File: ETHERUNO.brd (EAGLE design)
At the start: 68.6 x 53.3 mm, 98 parts, among them IC1 MC33269DT-5.0, IC2 APX811-44UG-7, IC3 ATMEGA16U2-MU, IC4 LM358D, IC5 ATMEGA328P TQFP32, IC7 MCP24AA025E48, IC8 W5500, J1 DC_2_1MM, P1 USB-6PSMT, P2 ICSP:MAIN, P3 ICSP:USB, P4 microSD, Q1 FDN340P, Q2 2N7002, Q3 2N7002, U1 HY931147C-RJ45, X1 16MHz, X2 25MHz, X3 16MHz

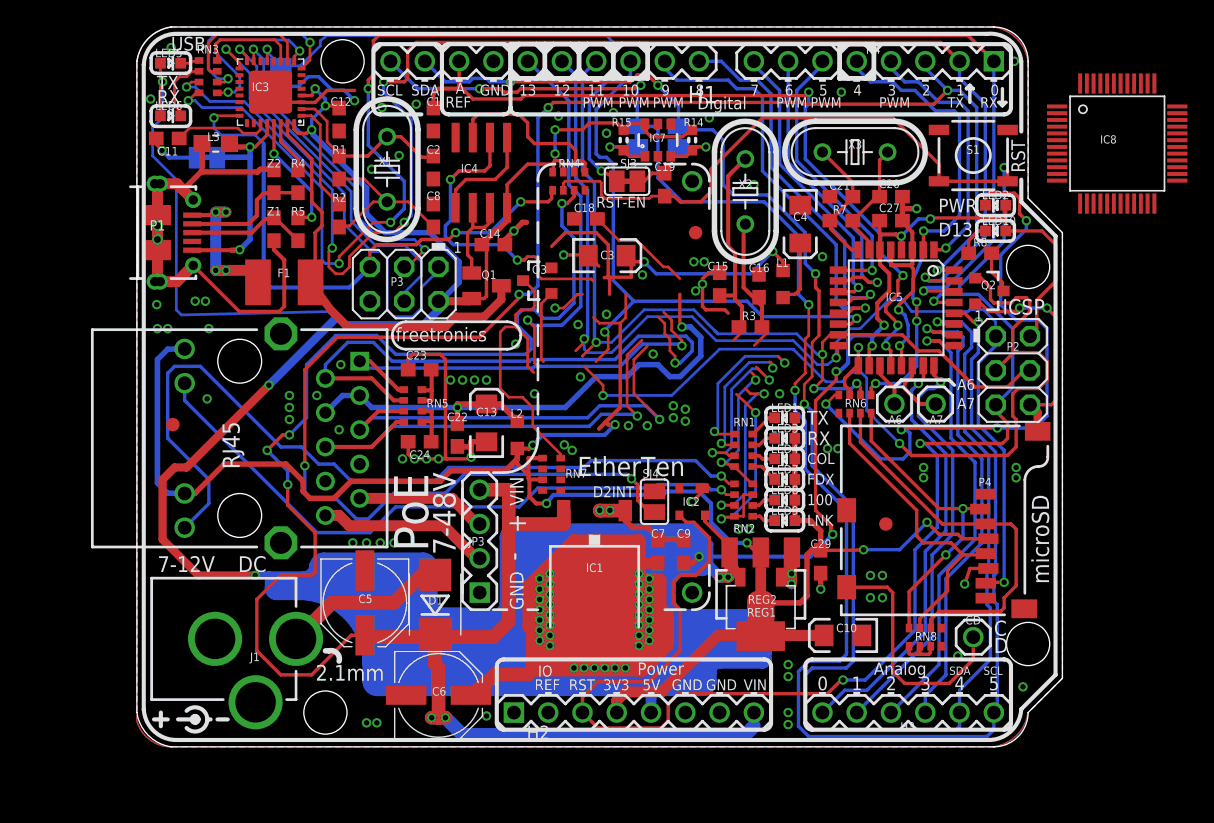
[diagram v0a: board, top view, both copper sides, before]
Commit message: Beginning of conversion to USB-C and W5100S
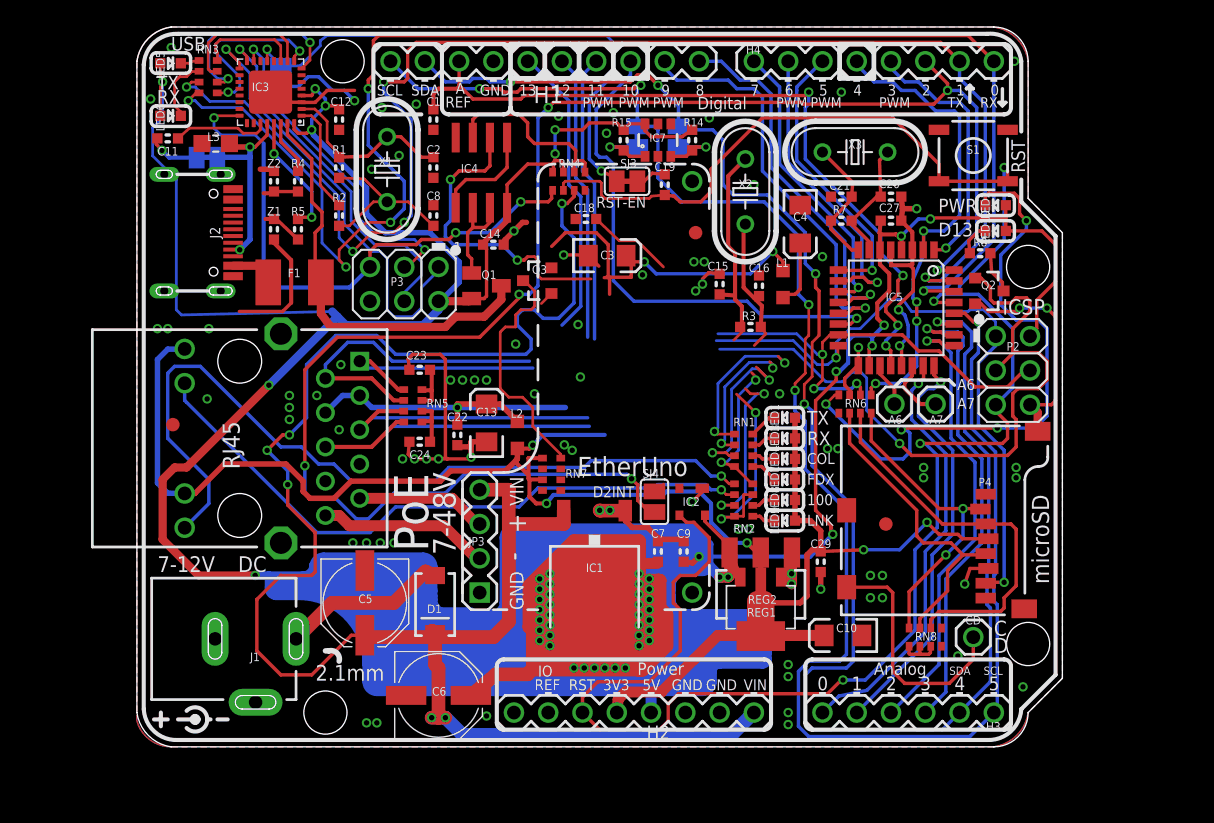
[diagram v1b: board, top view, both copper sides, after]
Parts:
- removed IC8: W5500, W5500:W5500
- removed P1: USB-6PSMT, freetronics-jon:USB-MICROB-MB05PMXX
- added J2: USB-C-16P-16P, SuperHouse-Connectors:USB-C-16P
- C1, C11, C12, C14, C15, C16, C18, C19, C2, C20, C21, C22, C23, C24, C27, C29, C7, C8, C9: device freetronics:0603 -> SuperHouse-DiscreteSemi:C0603
- C10, C13, C3, C4: device freetronics:EIA3216 -> SuperHouse-DiscreteSemi:EIA3216
- C5, C6: device rcl:PANASONIC_D -> SuperHouse-DiscreteSemi:PANASONIC_D
- D1: device freetronics:SMB-DIODE -> SuperHouse-DiscreteSemi:SMA-DIODE
- F1: device rcl:L1812 -> SuperHouse-Fuses:1812
- H1: device freetronics-original:1X10 -> SuperHouse-Connectors:1X10-S
- H2: device freetronics-master-v1:1X08 -> SuperHouse-Connectors:1X08-S
- H3: device freetronics:1X06 -> SuperHouse-Connectors:1X06-S
- H4: device freetronics:1X08 -> SuperHouse-Connectors:1X08-S
- IC5: device freetronics-2:TQFP32-08 -> SuperHouse-MCUs:TQFP32-08
- J1: device freetronics:POWER_JACK_PTH -> SuperHouse-Connectors:POWER_JACK_SLOTS
- LED1, LED10, LED2, LED3, LED4, LED5, LED6, LED7, LED8, LED9: device freetronics:LED-0603 -> SuperHouse-LEDs:LED-0603
- P2, P3: device pinhead:2X03 -> SuperHouse-Connectors:2X03-ICSP
- P4: device freetronics-master-v1:MICRO-SD-SOCKET-PP -> SuperHouse-Connectors:MICRO-SD-SOCKET-PP
- Q2, Q3: device freetronics:SOT23-3 -> SuperHouse-DiscreteSemi:SOT23-3
- R1, R2, R3, R4, R5, R7, R8: device freetronics:0603 -> SuperHouse-DiscreteSemi:R0603
- R14, R15: device freetronics-master-v1.1:0603 -> SuperHouse-DiscreteSemi:R0603
- RN1, RN2, RN3, RN5, RN6, RN7, RN8: device freetronics-master-v1:CAY16 -> SuperHouse-DiscreteSemi:CAY16
- S1: device freetronics:TACTILE_SWITCH_SMD -> SuperHouse-Switches:TACTILE_SMT-6MM
- SJ5, SJ6: value (none) -> SJCN
- U1: device freetronics-jon:HY931147C -> SuperHouse-Connectors:HY931147C
- X1, X2, X3: device freetronics-master-v1:HC49U-V -> SuperHouse-Oscillators:HC49U-V
- Z1, Z2: device freetronics:0603 -> SuperHouse-DiscreteSemi:TVS0603
- moved H1 11.4 mm to (30.2, 50.8)
- moved H4 8.89 mm to (54.6, 50.8)
- moved H2 8.89 mm to (36.8, 2.54)
- moved H3 6.35 mm to (57.1, 2.54)
- moved F1 0.76 mm to (11.7, 34.4)
- turned D1 to 270 degrees
- turned LED1 to 180 degrees
- turned LED10 to 180 degrees
- turned LED2 to 180 degrees
- turned LED3 to 180 degrees
- turned LED4 to 180 degrees
- turned LED5 to 0 degrees
- turned LED6 to 0 degrees
- turned LED7 to 180 degrees
- turned LED8 to 180 degrees
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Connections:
- net GND: now also J2.A12B1, J2.A1B12, J2.FIX1, J2.FIX2, J2.FIX3, J2.FIX4
- net N$115: now also J2.A4B9, J2.A9B4; no longer P1.VBUS
- net N$16: now also J2.A6, J2.B6; no longer P1.D+
- net N$17: now also J2.A7, J2.B7; no longer P1.D-
- net N$9: no longer P1.FIX1, P1.FIX2, P1.PIN1, P1.PIN2, P1.TAB1, P1.TAB2
- net USBGND: no longer P1.GND
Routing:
- net N$9: track 37.7 -> 10.4 mm, vias 2 -> 0
- net 3V3A: track 52.5 -> 33.1 mm, vias 2 -> 1
- net RXIN: track 43.1 -> 23.9 mm, vias 1 -> 0
- net D13_SCK: track 98.9 -> 79.8 mm, vias 4 -> 2
- net 3V3D: track 176.7 -> 161.7 mm, vias 8 -> 7
- net RXIP: track 32.1 -> 17.2 mm, vias 1 -> 0
- net D12_MISO: track 83.4 -> 69.3 mm, vias 3 -> 2
- net TXOP: track 33.9 -> 21.1 mm, vias 1 -> 0
- net D11_MOSI: track 68.2 -> 55.5 mm, vias 4 -> 3
- net TXON: track 37.1 -> 26.8 mm, vias 1 -> 0
- net D10_SS: track 50.1 -> 39.9 mm, vias 2 -> 1
- net N$115: track 12.3 -> 3.59 mm, vias 4 -> 0
- net N$17: track 9.47 -> 2.63 mm
- net GND: track 105.6 -> 99.3 mm, vias 98 -> 86
- net N$16: track 9.00 -> 3.10 mm
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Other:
- board text added: "EtherUno"
- board text added: "by Jonathan Oxer"
- board text added: "v4.0"
- board text added: "www.superhouse.tv/eu"
- board text removed: "EtherTen"
- board text removed: "by Marc Alexander and Jonathan Oxer"
- board text removed: "freetronics"
- board text removed: "v3.0"
- board text removed: "www.freetronics.com/et"

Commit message: Added cut-track jumper to isolate D4
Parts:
- added U$8: SJC-NORMAL, SuperHouse-Jumpers:SJC
- moved RN6 0.51 mm to (53.2, 24.9)
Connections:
- new net N$27: RN6.5, U$8.1
- net D4: now also U$8.2; no longer RN6.5
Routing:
- net D12_MISO: track 69.3 -> 65.5 mm
- net D4: track 36.2 -> 32.6 mm, vias 4 -> 3
- net D11_MOSI: track 55.5 -> 52.2 mm
- net N$27: track 0.00 -> 2.79 mm, vias 0 -> 1
- net D13_SCK: track 79.8 -> 77.0 mm
- net 3V3D: track 161.7 -> 159.2 mm
- net TXOP: track 21.1 -> 18.6 mm
- net TXON: track 26.8 -> 24.2 mm
- net 3V3A: track 33.1 -> 31.9 mm
- net N$25: track 29.0 -> 28.5 mm
- net N$24: track 23.6 -> 23.1 mm
- net N$20: track 22.7 -> 22.2 mm

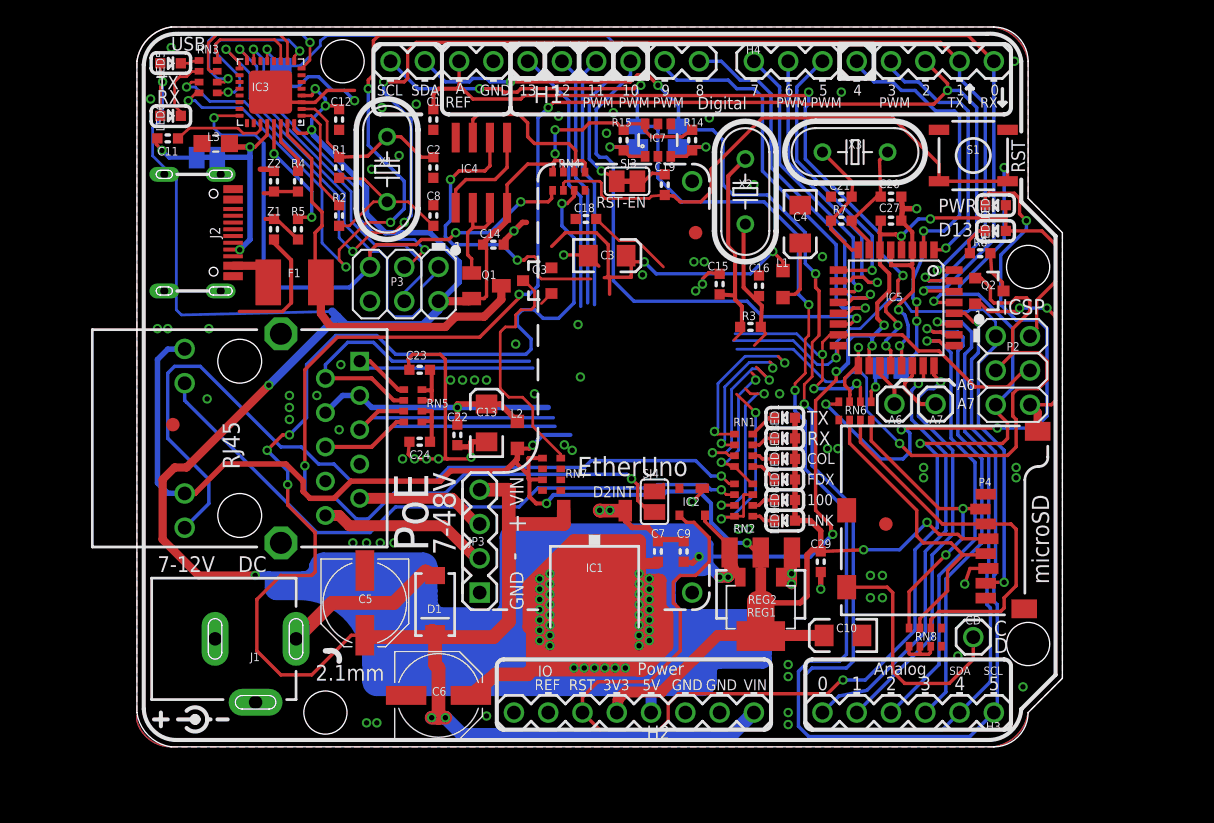
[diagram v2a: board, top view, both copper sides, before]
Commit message: Major rework of schematic to suit W6100
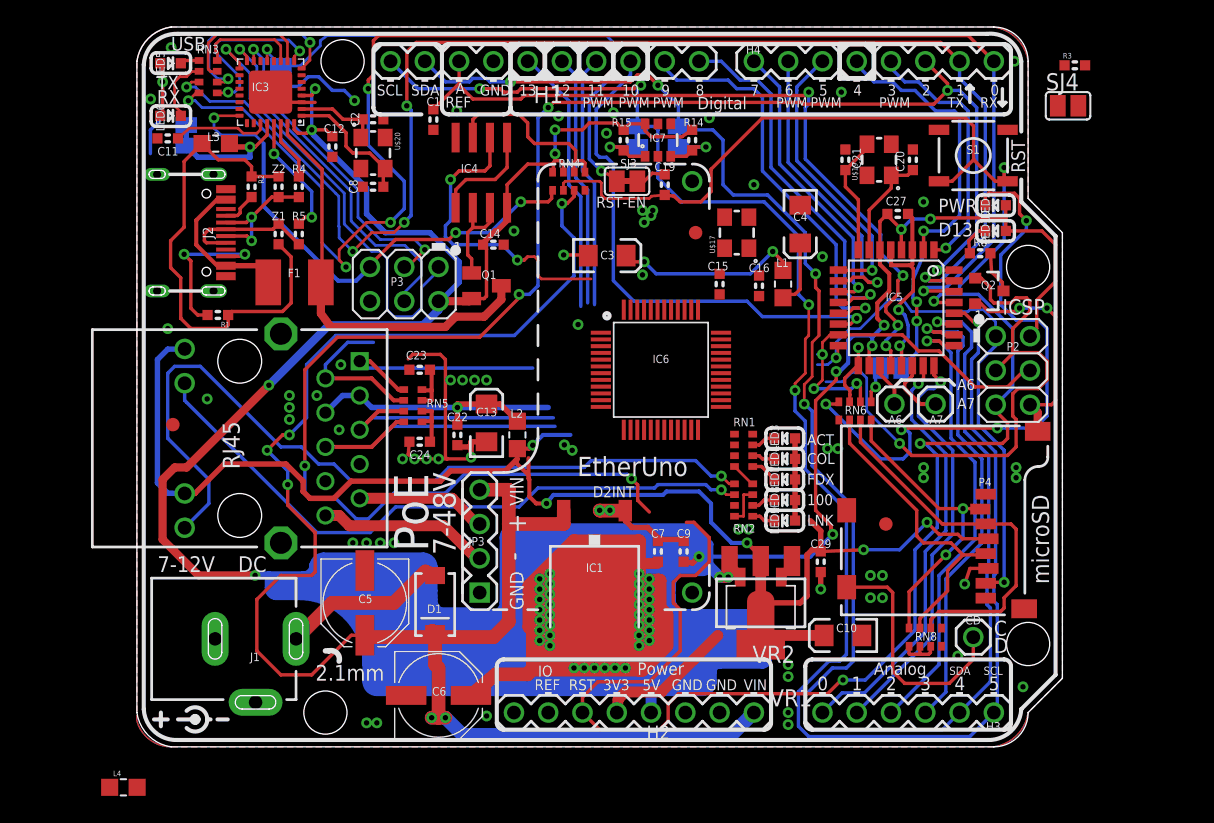
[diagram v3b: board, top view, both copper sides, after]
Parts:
- removed C18: 10nF, SuperHouse-DiscreteSemi:C0603
- removed IC2: APX811-44UG-7, freetronics-master-v1:SOT143-R
- removed LED1: YELLOW, SuperHouse-LEDs:LED-0603
- removed Q3: 2N7002, SuperHouse-DiscreteSemi:SOT23-3
- removed R7: 1M 0603, SuperHouse-DiscreteSemi:R0603
- removed REG1: LD1117-SOT89, freetronics:SOT89
- removed REG2: LD1117-SOT223, freetronics:SOT223
- removed RN7: 1K, SuperHouse-DiscreteSemi:CAY16
- removed X1, X3: 16MHz, SuperHouse-Oscillators:HC49U-V
- removed X2: 25MHz, SuperHouse-Oscillators:HC49U-V
- added IC6: W6100-LQFP, SuperHouse-ICs:LQFP48
- added L4: 1uH 250mA 0805, SuperHouse-DiscreteSemi:0805-LARGE
- added U$17, U$19, U$20: CRYSTAL-GND3X2, SuperHouse-Oscillators:CRYSTAL-SMD-3X2
- added VR1: LD1117-SOT223, SuperHouse-Regulators:SOT-223
- added VR2: LD1117-SOT89, SuperHouse-Regulators:SOT89
- A6, A7, CD: value M01PTH -> M01; device freetronics-2:1X01 -> SuperHouse-Connectors:1X01
- FID1, FID2, FID3: device freetronics:FIDUCIAL-1X2.5 -> SuperHouse-Symbols:FIDUCIAL-1X2.5
- IC1: device linear:DPACK -> SuperHouse-Regulators:DPACK
- IC3: device freetronics-jon:ATMEL_QFN32 -> SuperHouse-MCUs:ATMEL_QFN32
- L1, L2: device rcl:L2012C -> SuperHouse-DiscreteSemi:0805-LARGE
- L3: device freetronics-master-v1:0805-LARGE -> SuperHouse-DiscreteSemi:0805-LARGE
- R1: value 1M 0603 -> 4K7
- R2: value 27R 0603 -> 4K7
- R3: value 1M -> (none)
- R4, R5: value 22R 0603 -> 22R
- RN1, RN2: value 1K -> 330R
- RN4: device freetronics-master-v1:CAY16 -> SuperHouse-DiscreteSemi:CAY16
- SJ1, SJ3: device jumper:SJ -> SuperHouse-Jumpers:SJC
- SJ2: device jumper:SJ -> SuperHouse-Jumpers:SJ
- SJ4: value D2_INT -> (none); device jumper:SJ -> SuperHouse-Jumpers:SJ
- SJ5, SJ6: value SJCN -> SJC; device freetronics-jon:SJC -> SuperHouse-Jumpers:SJC
- SJ7: value SJC-NORMAL -> SJC
- moved SJ4 42.4 mm to (69.0, 47.5), turned to 0 degrees
- moved R3 30.9 mm to (69.5, 50.5)
- moved R1 14.1 mm to (6.00, 32.0), turned to 180 degrees
- moved R2 6.83 mm to (8.50, 41.5)
- moved C2 5.72 mm to (17.5, 46.5), turned to 180 degrees
- moved C8 4.95 mm to (17.5, 41.5), turned to 0 degrees
- moved C20 3.18 mm to (57.5, 43.5), turned to 270 degrees
- moved C21 2.75 mm to (52.5, 43.5), turned to 270 degrees
- moved SJ1 2.26 mm to (3.66, 45.3), turned to 90 degrees
- moved C12 2.06 mm to (14.5, 44.5)
- moved C27 0.71 mm to (56.4, 39.5)
- moved Z2 0.53 mm to (10.5, 41.5)
- moved J2 0.53 mm to (1.50, 38.1)
- moved Z1 0.49 mm to (10.5, 38.0)
- moved R4 0.41 mm to (12.0, 41.5)
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- renumbered U$8 to SJ7
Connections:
- removed net 1V8A: C4.A, L1.2
- removed net 1V8_OUT: C3.A, L1.1
- removed net INT: SJ4.2
- removed net N$113: C2.2, IC3.2, R1.2, X1.2
- removed net N$114: C8.2, R1.1, R2.2, X1.1
- removed net N$330: LED1.C, RN1.8
- removed net SEN: Q3.3, RN7.4
- removed net WIZRST: IC2.2
- removed net WRXLED: RN1.2
- removed net WTXLED: RN1.1
- removed net XTLN: C16.1, R3.2, X2.2
- removed net XTLP: C15.1, R3.1, X2.1
- new net 1V2A: C4.A, IC6.4, L1.2
- new net 1V2D: C3.A, IC6.13, IC6.22, IC6.31, IC6.45, L4.2
- new net 1V2O: IC6.14, L1.1, L4.1
- new net 3.3V: C10.A, IC4.2, IC6.24, IC6.36, L2.1, LED3.A, LED4.A, LED7.A, LED8.A, LED9.A, U1.P$11, U1.P$13, VR1.2, VR1.4, VR2.2, VR2.4
- new net ACTLED: IC6.20, RN1.2
- new net MODE: IC6.25, R3.2, SJ4.1
- new net N$10: J2.B5, R1.2
- new net N$30: C15.1, IC6.11, U$17.1
- new net N$31: C2.2, IC3.2, U$20.1
- new net N$32: C16.1, IC6.12, U$17.3
- new net N$33: IC6.29
- new net N$34: J2.A5, R2.2
- net 3V3A: now also IC6.15, IC6.8; no longer C18.1
- net 3V3D: now also SJ4.2; no longer C10.A, IC4.2, L2.1, LED1.A, LED3.A, LED4.A, LED7.A, LED8.A, LED9.A, REG1.2, REG1.4, REG2.2, REG2.4, RN7.5, U1.P$11, U1.P$13
- net 5V: now also VR1.3, VR2.3; no longer IC2.4, REG1.3, REG2.3
- net COLLED: now also IC6.21
- net D10_SS: no longer Q3.1
- net D11_MOSI: now also IC6.32
- net D12_MISO: now also IC6.33
- net D13_SCK: now also IC6.30
- net D2: no longer SJ4.1
- net FDXLED: now also IC6.19
- net GND: now also IC6.1, IC6.10, IC6.16, IC6.23, IC6.26, IC6.27, IC6.28, IC6.46, IC6.7, R3.1, U$17.2, U$17.4, U$19.2, U$19.4, U$20.2, U$20.4, VR1.1, VR2.1; no longer C18.2, IC2.1, J2.A12B1, J2.A1B12, J2.FIX1, J2.FIX2, J2.FIX3, J2.FIX4, Q3.2, REG1.1, REG2.1
- net LINKLED: now also IC6.17
- net N$2: now also U$19.1; no longer R7.2, X3.2
- net N$7: now also U$19.3; no longer R7.1, X3.1
- net N$8: now also C8.2, U$20.3; no longer R2.1
- net N$9: now also J2.A12B1, J2.A1B12, J2.FIX1, J2.FIX2, J2.FIX3, J2.FIX4, R1.1, R2.1
- net RESET: now also IC6.48; no longer IC2.3
- net RXIN: now also IC6.5
- net RXIP: now also IC6.6
- net SPDLED: now also IC6.18
- net TXON: now also IC6.2
- net TXOP: now also IC6.3
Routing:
- net 3V3D: track 159.2 -> 34.7 mm, vias 7 -> 2
- net 3.3V: track 0.00 -> 108.7 mm, vias 0 -> 5
- net 5V: track 1240.7 -> 1210.8 mm, vias 53 -> 52
- net 1V8_OUT: track 26.5 -> 0.00 mm, vias 2 -> 0
- net N$9: track 10.4 -> 35.8 mm
- net GND: track 99.3 -> 80.3 mm, vias 86 -> 73
- net SEN: track 17.9 -> 0.00 mm
- net XTLP: track 16.0 -> 0.00 mm
- net 1V2O: track 0.00 -> 13.8 mm, vias 0 -> 2
- net N$113: track 13.5 -> 0.00 mm
- net SPDLED: track 13.0 -> 0.08 mm, vias 2 -> 0
- net COLLED: track 12.7 -> 0.00 mm, vias 2 -> 0
- net N$114: track 12.7 -> 0.00 mm
- net LINKLED: track 15.4 -> 3.06 mm, vias 2 -> 0
- net RXIN: track 23.9 -> 11.7 mm
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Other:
- board text added: "ACT"
